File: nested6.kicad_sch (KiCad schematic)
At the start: 3 parts, among them U4 XL1509-3.3

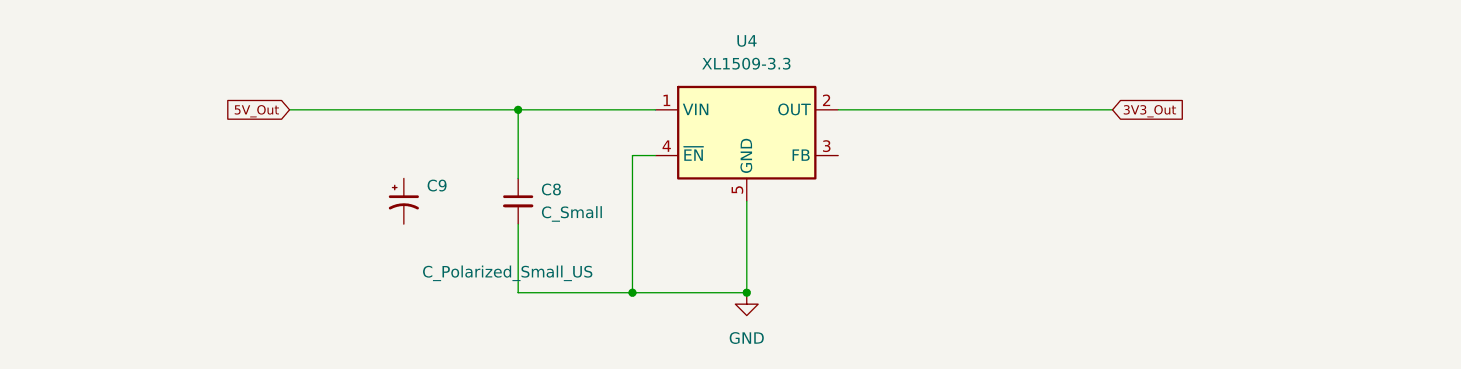
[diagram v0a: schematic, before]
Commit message: Removed old backups and updated KiCad files
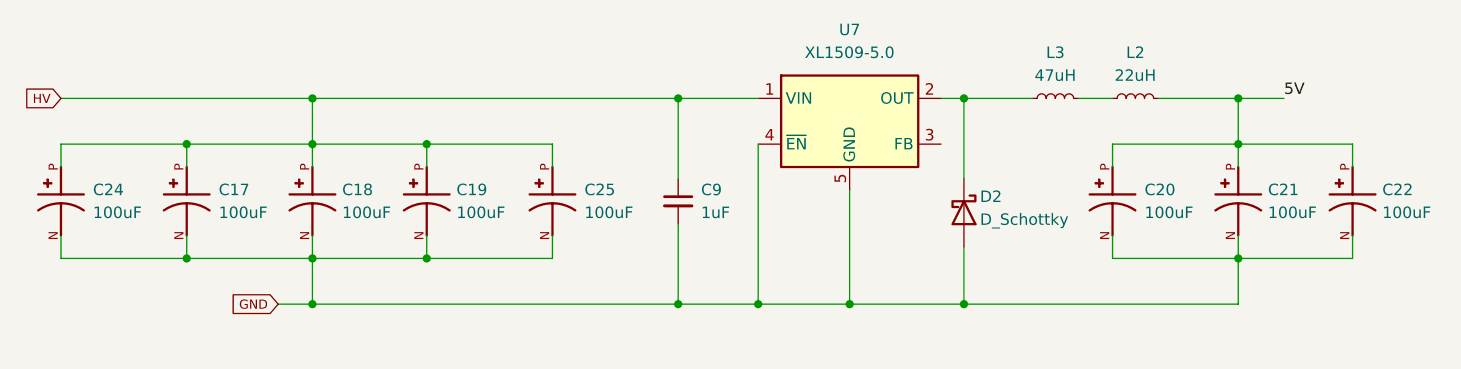
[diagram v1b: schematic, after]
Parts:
- removed C8: C_Small, Capacitor_SMD:C_1206_3216Metric_Pad1.33x1.80mm_HandSolder, symbol Device:C_Small
- removed C9: C_Polarized_Small_US, symbol Device:C_Polarized_Small_US
- removed U4: XL1509-3.3, Package_SO:SOIC-8_3.9x4.9mm_P1.27mm, symbol Regulator_Switching:XL1509-3.3
- added C17, C18, C19, C20, C21, C22, C24, C25: 100uF, TLJA107M006R0800:CAPPM3216X180N, symbol TLJA107M006R0800:TLJA107M006R0800
- added C9: 1uF, Capacitor_SMD:C_1206_3216Metric_Pad1.33x1.80mm_HandSolder, symbol Device:C_Small
- added D2: D_Schottky, Diode_SMD:D_SOD-123, symbol Device:D_Schottky
- added L2: 22uH, Inductor_SMD:L_0603_1608Metric_Pad1.05x0.95mm_HandSolder, symbol Device:L_Small
- added L3: 47uH, Inductor_SMD:L_0805_2012Metric_Pad1.05x1.20mm_HandSolder, symbol Device:L_Small
- added U7: XL1509-5.0, Package_SO:SOIC-8_3.9x4.9mm_P1.27mm, symbol Regulator_Switching:XL1509-5.0
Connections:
- net GND: now also C17.N, C18.N, C19.N, C20.N, C21.N, C22.N, C24.N, C25.N, C9.2, D2.2 (A), U7.4 (~{EN}), U7.5 (GND), U7.6 (GND), U7.7 (GND), U7.8 (GND)
- new net: D2.1 (K), L3.1, U7.2 (OUT)
- new net: L2.1, L3.2
- new net 5V: C20.P, C21.P, C22.P, L2.2
- new net HV: C17.P, C18.P, C19.P, C24.P, C25.P, C9.1, U7.1 (VIN)

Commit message: added circuits
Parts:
- added Q1: NMOS, Package_TO_SOT_SMD:SOT-23, symbol Simulation_SPICE:NMOS
- added R14: 5.1k, Resistor_SMD:R_0805_2012Metric_Pad1.20x1.40mm_HandSolder, symbol Device:R_Small_US
- added R15: 390, Resistor_SMD:R_0805_2012Metric_Pad1.20x1.40mm_HandSolder, symbol Device:R_Small_US
- added R16: 2.7k, Resistor_SMD:R_0805_2012Metric_Pad1.20x1.40mm_HandSolder, symbol Device:R_Small_US
- added U8: TP4056-42-ESOP8, Package_SO:SOIC-8-1EP_3.9x4.9mm_P1.27mm_EP2.41x3.3mm_ThermalVias, symbol Battery_Management:TP4056-42-ESOP8
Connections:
- net 5V: now also U8.4 (V_{CC})
- net GND: now also Q1.3 (S), R15.2, U8.3 (GND)
- new net: R14.1, R16.1, U8.2 (PROG)
- new net: R14.2, R15.1
- new net: Q1.1 (D), R16.2
- new net Battery: U8.5 (BAT)
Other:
- moved on the sheet: C17, C18, C19, C20, C21, C22, C24, C25, C9, D2, L2, L3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

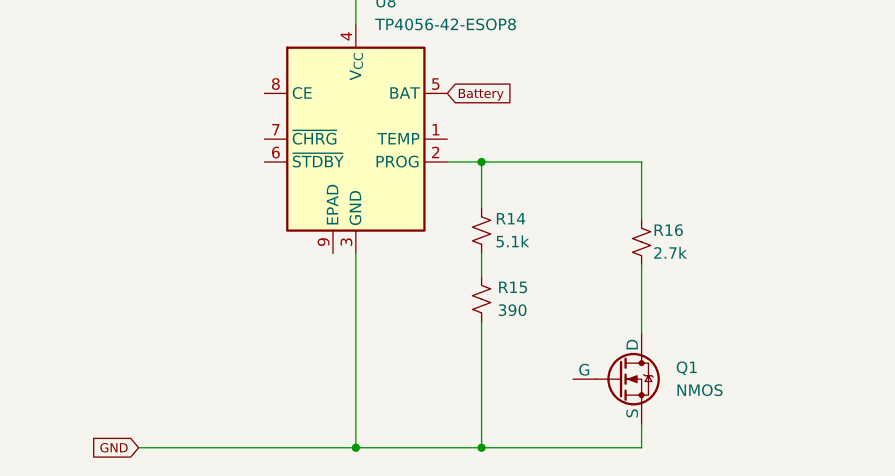
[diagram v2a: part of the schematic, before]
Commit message: Removed old backups and updated KiCad files
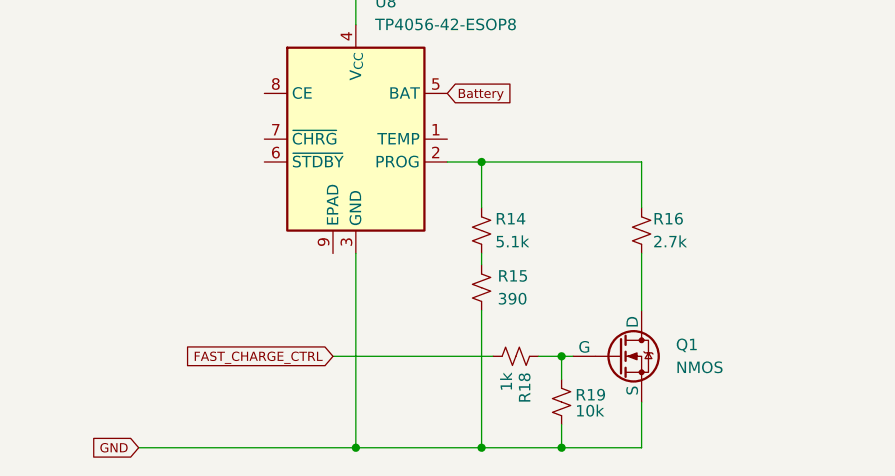
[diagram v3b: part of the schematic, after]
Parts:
- added R18: 1k, Resistor_SMD:R_0805_2012Metric_Pad1.20x1.40mm_HandSolder, symbol Device:R_Small_US
- added R19: 10k, Resistor_SMD:R_0805_2012Metric_Pad1.20x1.40mm_HandSolder, symbol Device:R_Small_US
- U8: footprint Package_SO:SOIC-8-1EP_3.9x4.9mm_P1.27mm_EP2.41x3.3mm_ThermalVias -> TP4056-42-ESOP8:SOIC127P600X175-9N
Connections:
- net GND: now also R19.2
- net at Q1.2 (G): now also R18.1, R19.1
- new net FAST_CHARGE_CTRL: R18.2
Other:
- moved on the sheet: Q1, R15, R16

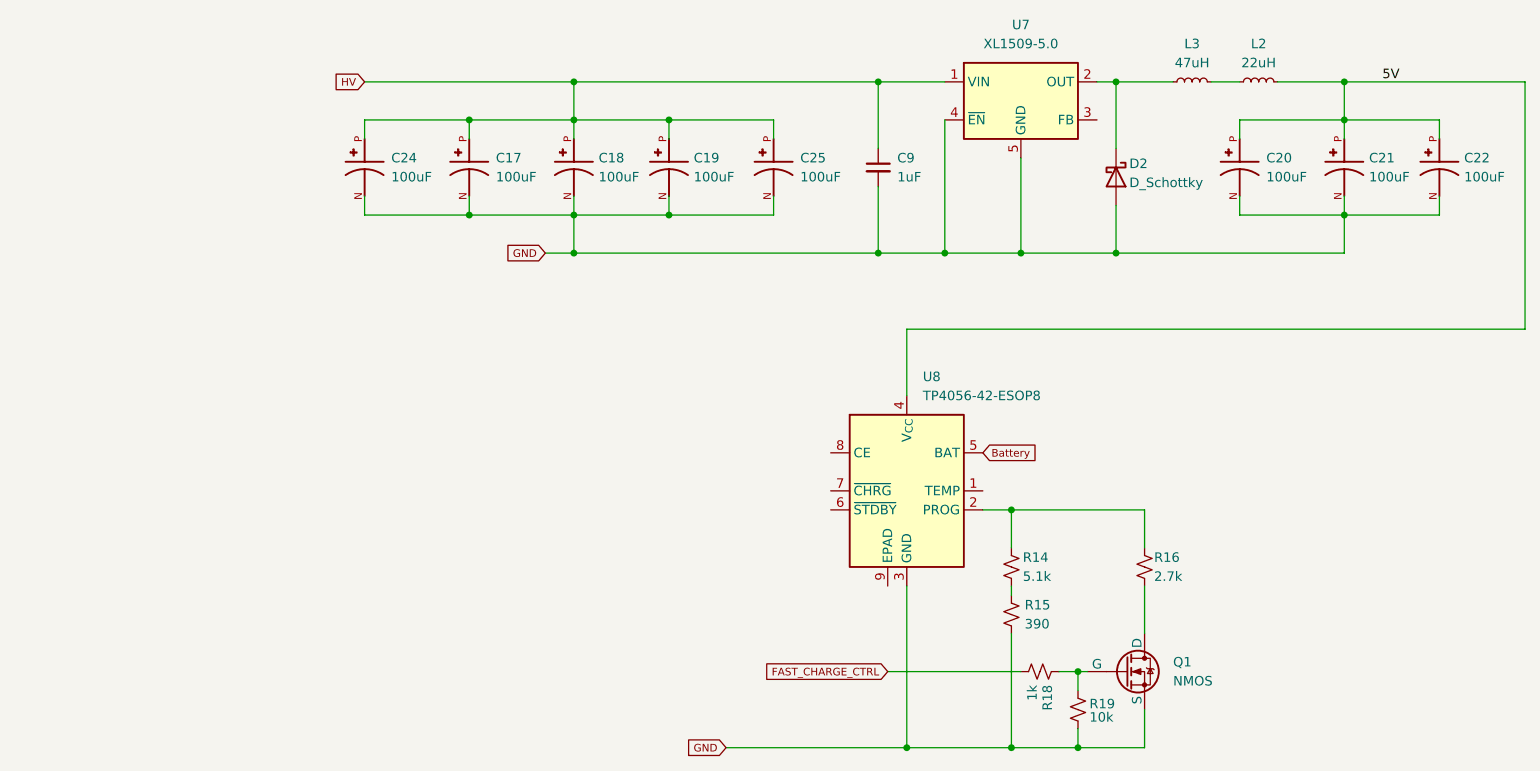
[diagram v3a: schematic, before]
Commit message: Removed old backups and updated KiCad files
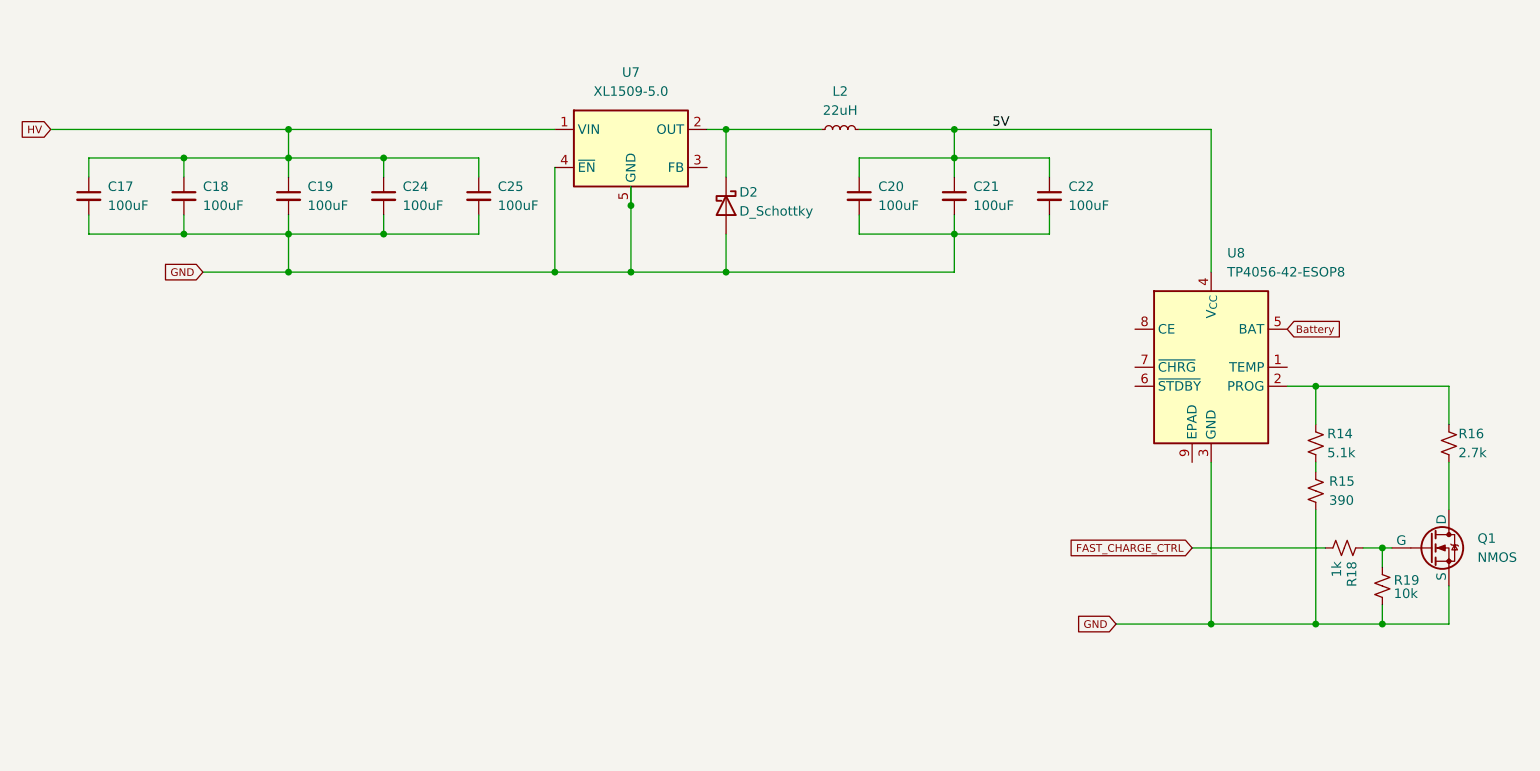
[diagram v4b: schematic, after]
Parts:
- removed C17, C18, C19, C20, C21, C22, C24, C25: 100uF, TLJA107M006R0800:CAPPM3216X180N, symbol TLJA107M006R0800:TLJA107M006R0800
- removed C9: 1uF, Capacitor_SMD:C_1206_3216Metric_Pad1.33x1.80mm_HandSolder, symbol Device:C_Small
- removed L3: 47uH, Inductor_SMD:L_0805_2012Metric_Pad1.05x1.20mm_HandSolder, symbol Device:L_Small
- added C17, C18, C19, C20, C21, C22, C24, C25: 100uF, Capacitor_SMD:C_1206_3216Metric_Pad1.33x1.80mm_HandSolder, symbol Device:C_Small
- R15, R18: footprint Resistor_SMD:R_0805_2012Metric_Pad1.20x1.40mm_HandSolder -> Resistor_SMD:R_0603_1608Metric_Pad0.98x0.95mm_HandSolder
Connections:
- net 5V: now also C20.1, C21.1, C22.1
- net GND: now also C17.2, C18.2, C19.2, C20.2, C21.2, C22.2, C24.2, C25.2
- net HV: now also C17.1, C18.1, C19.1, C24.1, C25.1
- net at D2.1 (K), U7.2 (OUT): now also L2.1
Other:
- moved on the sheet: D2, L2, Q1, R14, R15, R16, R18, R19, U7, U8

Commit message: Removed old backups and updated KiCad files
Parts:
- C17, C18, C19, C20, C21, C22, C24, C25: LCSC (none) -> C15008
- D2: LCSC (none) -> C727113
- L2: LCSC (none) -> C361669
- Q1: LCSC (none) -> C22446827
- R14: LCSC (none) -> C27834
- R15: LCSC (none) -> C23151
- R16: LCSC (none) -> C17530
- R18: LCSC (none) -> C21190
- R19: LCSC (none) -> C17902
- U7: LCSC (none) -> C61063
- U8: LCSC (none) -> C16581
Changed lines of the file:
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@@
+			)
+		)
+		(property "LCSC" "C17902"
+			(at 205.74 95.25 0)
+			(effects
+				(font
+					(size 1.27 1.27)
+				)
+				(hide yes)
 			)
 		)
@@
 			)
 		)
+		(property "LCSC" "C21190"
+			(at 200.66 90.17 0)
+			(effects
+				(font
+					(size 1.27 1.27)
+				)
+				(hide yes)
+			)
+		)
 		(pin "2"
 		)
@@
 		)
 		(property "Description" "Resistor, small US symbol"
+			(at 196.85 76.2 0)
+			(effects
+				(font
+					(size 1.27 1.27)
+				)
+				(hide yes)
+			)
+		)
+		(property "LCSC" "C27834"
 			(at 196.85 76.2 0)
 			(effects
@@
 			)
 		)
+		(property "LCSC" "C15008"
+			(at 45.72 43.18 0)
+			(effects
+				(font
+					(size 1.27 1.27)
+				)
+				(hide yes)
+			)
+		)
 		(pin "1"
 		)
@@
 			)
 		)
+		(property "LCSC" "C15008"
+			(at 135.89 43.18 0)
+			(effects
+				(font
+					(size 1.27 1.27)
+				)
+				(hide yes)
+			)
+		)
 		(pin "1"
 		)
@@
 			)
 		)
+		(property "LCSC" "C15008"
+			(at 148.59 43.18 0)
+			(effects
+				(font
+					(size 1.27 1.27)
+				)
+				(hide yes)
+			)
+		)
 		(pin "1"
 		)
@@
 			)
 		)
+		(property "LCSC" "C15008"
+			(at 85.09 43.18 0)
+			(effects
+				(font
+					(size 1.27 1.27)
+				)
+				(hide yes)
+			)
+		)
 		(pin "1"
 		)
@@
 			)
 		)
+		(property "LCSC" "C15008"
+			(at 161.29 43.18 0)
+			(effects
+				(font
+					(size 1.27 1.27)
+				)
+				(hide yes)
+			)
+		)
 		(pin "1"
 		)
@@
 			)
 		)
+		(property "LCSC" "C361669"
+			(at 133.35 34.29 90)
+			(effects
+				(font
+					(size 1.27 1.27)
+				)
+				(hide yes)
+			)
+		)
 		(pin "1"
 		)
@@
 		)
 		(property "Description" "Resistor, small US symbol"
+			(at 214.63 76.2 0)
+			(effects
+				(font
+					(size 1.27 1.27)
+				)
+				(hide yes)
+			)
+		)
+		(property "LCSC" "C17530"
 			(at 214.63 76.2 0)
 			(effects
@@
 			)
 		)
+		(property "LCSC" "C15008"
+			(at 59.69 43.18 0)
+			(effects
+				(font
+					(size 1.27 1.27)
+				)
+				(hide yes)
+			)
+		)
 		(pin "1"
 		)
@@
 			)
 		)
+		(property "LCSC" "C22446827"
+			(at 212.09 90.17 0)
+			(effects
+				(font
+					(size 1.27 1.27)
+				)
+				(hide yes)
+			)
+		)
 		(pin "3"
 		)
@@
 		(property "Description" "Schottky diode"
 			(at 118.11 44.45 0)
+			(effects
+				(font
+					(size 1.27 1.27)
+				)
+				(hide yes)
+			)
+		)
+		(property "LCSC" "C727113"
+			(at 118.11 44.45 90)
 			(effects
 				(font
@@
 			)
 		)
+		(property "LCSC" "C16581"
+			(at 182.88 66.04 0)
+			(effects
+				(font
+					(size 1.27 1.27)
+				)
+				(hide yes)
+			)
+		)
 		(pin "5"
 		)
@@
 			)
 		)
+		(property "LCSC" "C61063"
+			(at 105.41 36.83 0)
+			(effects
+				(font
+					(size 1.27 1.27)
+				)
+				(hide yes)
+			)
+		)
 		(pin "7"
 		)
@@
 			)
 		)
+		(property "LCSC" "C15008"
+			(at 72.39 43.18 0)
+			(effects
+				(font
+					(size 1.27 1.27)
+				)
+				(hide yes)
+			)
+		)
 		(pin "1"
 		)
@@
 			)
 		)
+		(property "LCSC" "C15008"
+			(at 33.02 43.18 0)
+			(effects
+				(font
+					(size 1.27 1.27)
+				)
+				(hide yes)
+			)
+		)
 		(pin "1"
 		)
@@
 			(at 196.85 82.55 0)
 			(effects
+				(font
+					(size 1.27 1.27)
+				)
+				(hide yes)
+			)
+		)
+		(property "LCSC" "C23151"
+			(at 196.85 82.55 0)
+			(effects

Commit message: Removed old backups and update KiCad files
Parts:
- added TP17, TP18: TestPoint, TestPoint:TestPoint_Pad_1.0x1.0mm, symbol Connector:TestPoint
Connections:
- net 5V: now also TP17.1
- net GND: now also TP18.1
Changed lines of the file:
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@@
+	)
+	(junction
+		(at 214.63 97.79)
+		(diameter 0)
+		(color 0 0 0 0)
 	)
 	(junction
@@
 	)
 	(junction
+		(at 170.18 34.29)
+		(diameter 0)
+		(color 0 0 0 0)
+	)
+	(junction
 		(at 196.85 100.33)
 		(diameter 0)
@@
 	(wire
 		(pts
+			(xy 214.63 97.79) (xy 214.63 100.33)
+		)
+		(stroke
+			(width 0)
+			(type default)
+		)
+	)
+	(wire
+		(pts
 			(xy 59.69 34.29) (xy 59.69 38.1)
 		)
@@
 	(wire
 		(pts
-			(xy 214.63 95.25) (xy 214.63 100.33)
+			(xy 214.63 95.25) (xy 214.63 97.79)
 		)
 		(stroke
@@
 	(wire
 		(pts
+			(xy 170.18 34.29) (xy 182.88 34.29)
+		)
+		(stroke
+			(width 0)
+			(type default)
+		)
+	)
+	(wire
+		(pts
 			(xy 118.11 48.26) (xy 118.11 53.34)
 		)
@@
 	(wire
 		(pts
-			(xy 148.59 34.29) (xy 182.88 34.29)
+			(xy 148.59 34.29) (xy 170.18 34.29)
 		)
 		(stroke
@@
 					(unit 1)
 				)
+			)
+		)
+	)
+	(symbol
+		(lib_id "Connector:TestPoint")
+		(at 170.18 34.29 0)
+		(unit 1)
+		(exclude_from_sim no)
+		(in_bom yes)
+		(on_board yes)
+		(dnp no)
+		(fields_autoplaced yes)
+		(property "Reference" "TP17"
+			(at 172.72 29.7179 0)
+			(effects
+				(font
+					(size 1.27 1.27)
+				)
+				(justify left)
+			)
+		)
+		(property "Value" "TestPoint"
+			(at 172.72 32.2579 0)
+			(effects
+				(font
+					(size 1.27 1.27)
+				)
+				(justify left)
+			)
+		)
+		(property "Footprint" "TestPoint:TestPoint_Pad_1.0x1.0mm"
+			(at 175.26 34.29 0)
+			(effects
+				(font
+					(size 1.27 1.27)
+				)
+				(hide yes)
+			)
+		)
+		(property "Datasheet" "~"
+			(at 175.26 34.29 0)
+			(effects
+				(font
+					(size 1.27 1.27)
+				)
+				(hide yes)
+			)
+		)
+		(property "Description" "test point"
+			(at 170.18 34.29 0)
+			(effects
+				(font
+					(size 1.27 1.27)
+				)
+				(hide yes)
+			)
+		)
+		(pin "1"
+		)
+		(instances
+			(project "EEE3088F Design project"
+				(path "/d1463c6f-2f5e-4460-8cd2-c7ccf4d8def7/eb0372fa-b1c5-4b6c-955d-8ba0b61c59ee"
+					(reference "TP17")
+					(unit 1)
+				)
+			)
+		)
+	)
+	(symbol
+		(lib_id "Connector:TestPoint")
+		(at 214.63 97.79 270)
+		(unit 1)
+		(exclude_from_sim no)
+		(in_bom yes)
+		(on_board yes)
+		(dnp no)
+		(fields_autoplaced yes)
+		(property "Reference" "TP18"
+			(at 219.71 96.5199 90)
+			(effects
+				(font
+					(size 1.27 1.27)
+				)
+				(justify left)
+			)
+		)
+		(property "Value" "TestPoint"
+			(at 219.71 99.0599 90)
+			(effects
+				(font
+					(size 1.27 1.27)
+				)
+				(justify left)
+			)
+		)
+		(property "Footprint" "TestPoint:TestPoint_Pad_1.0x1.0mm"
+			(at 214.63 102.87 0)
+			(effects
+				(font
+					(size 1.27 1.27)
+				)
+				(hide yes)
+			)
+		)
+		(property "Datasheet" "~"
+			(at 214.63 102.87 0)
+			(effects
+				(font
+					(size 1.27 1.27)
+				)
+				(hide yes)
+			)
+		)
+		(property "Description" "test point"
+			(at 214.63 97.79 0)
+			(effects
+				(font
+					(size 1.27 1.27)
+				)
+				(hide yes)
+			)
+		)
+		(pin "1"
+		)
+		(instances
+			(project "EEE3088F Design project"
+				(path "/d1463c6f-2f5e-4460-8cd2-c7ccf4d8def7/eb0372fa-b1c5-4b6c-955d-8ba0b61c59ee"
+					(reference "TP18")
+					(unit 1)
+				)
